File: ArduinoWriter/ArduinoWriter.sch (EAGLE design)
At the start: 11 parts, among them IC1 ATMEGA328-PU, IC2 TC74HC08AP, Q1 HUSG-16.000-20, SW1 SS-12D01-VG4, U1 ARRDUINOUNO-NOSILK

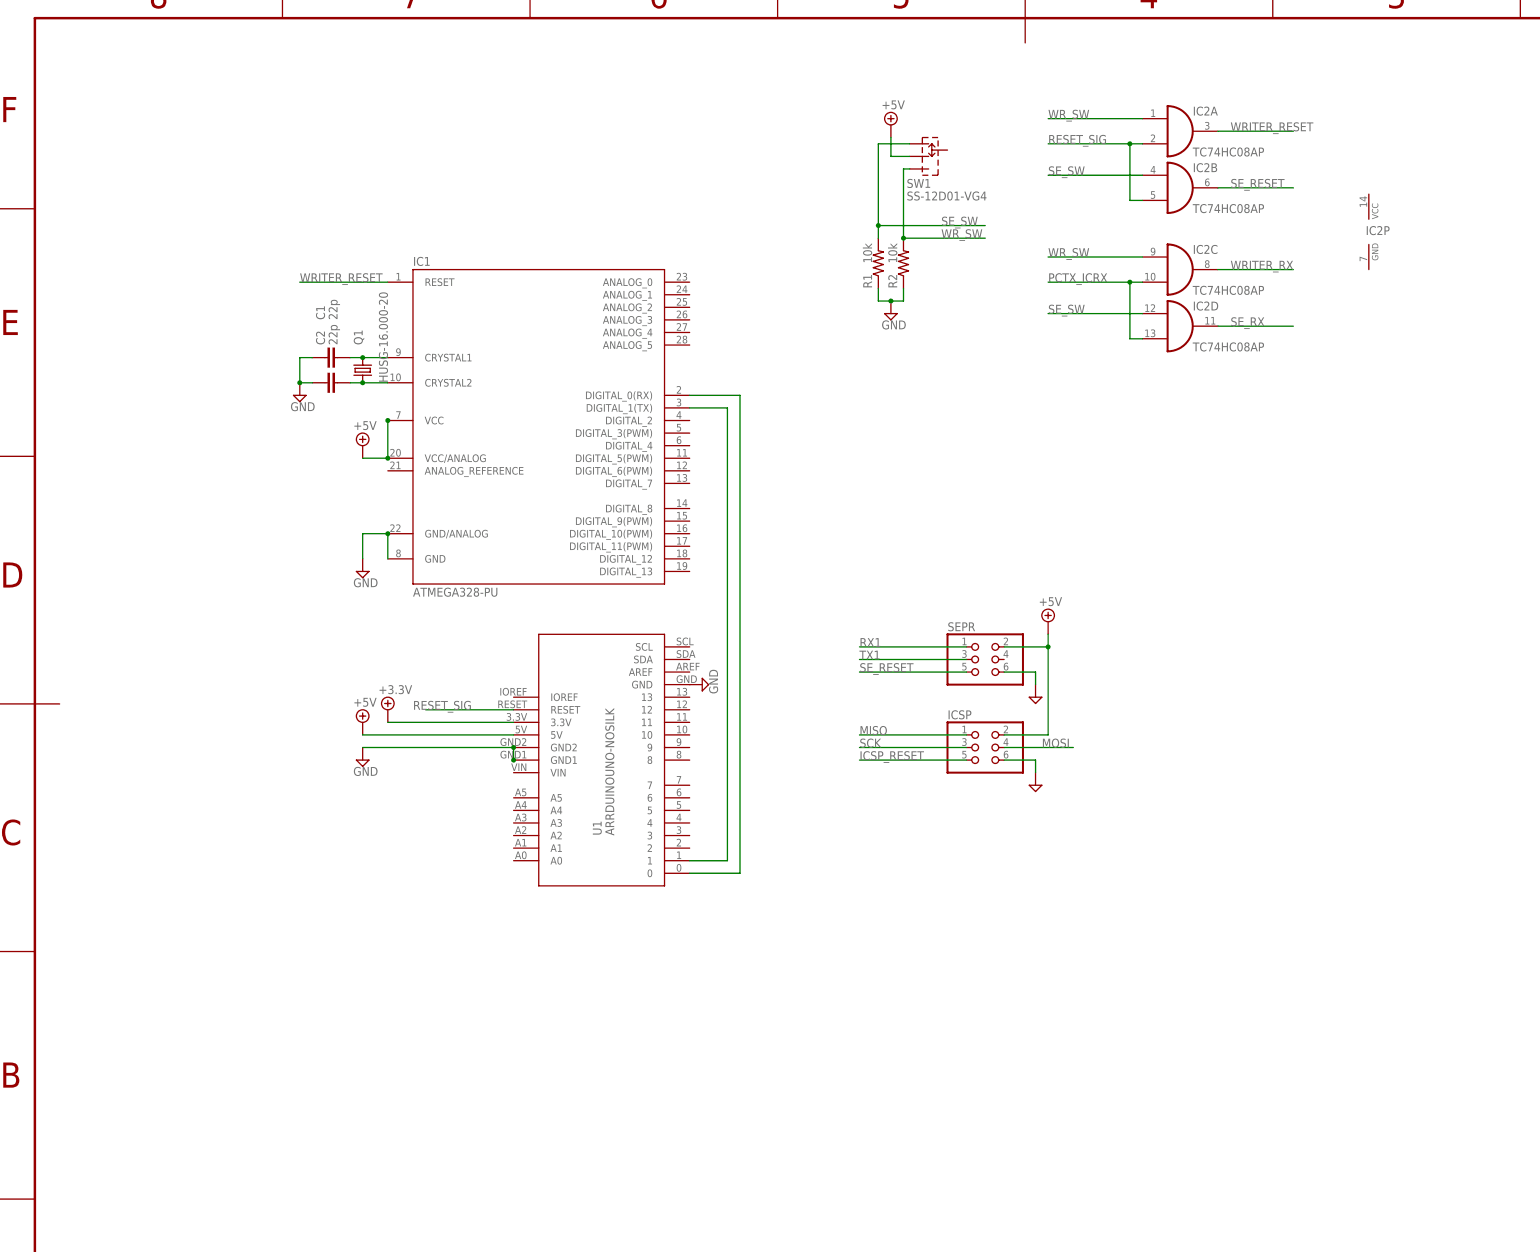
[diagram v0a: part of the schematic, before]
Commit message: SEWR_ICSP 切替回路実装
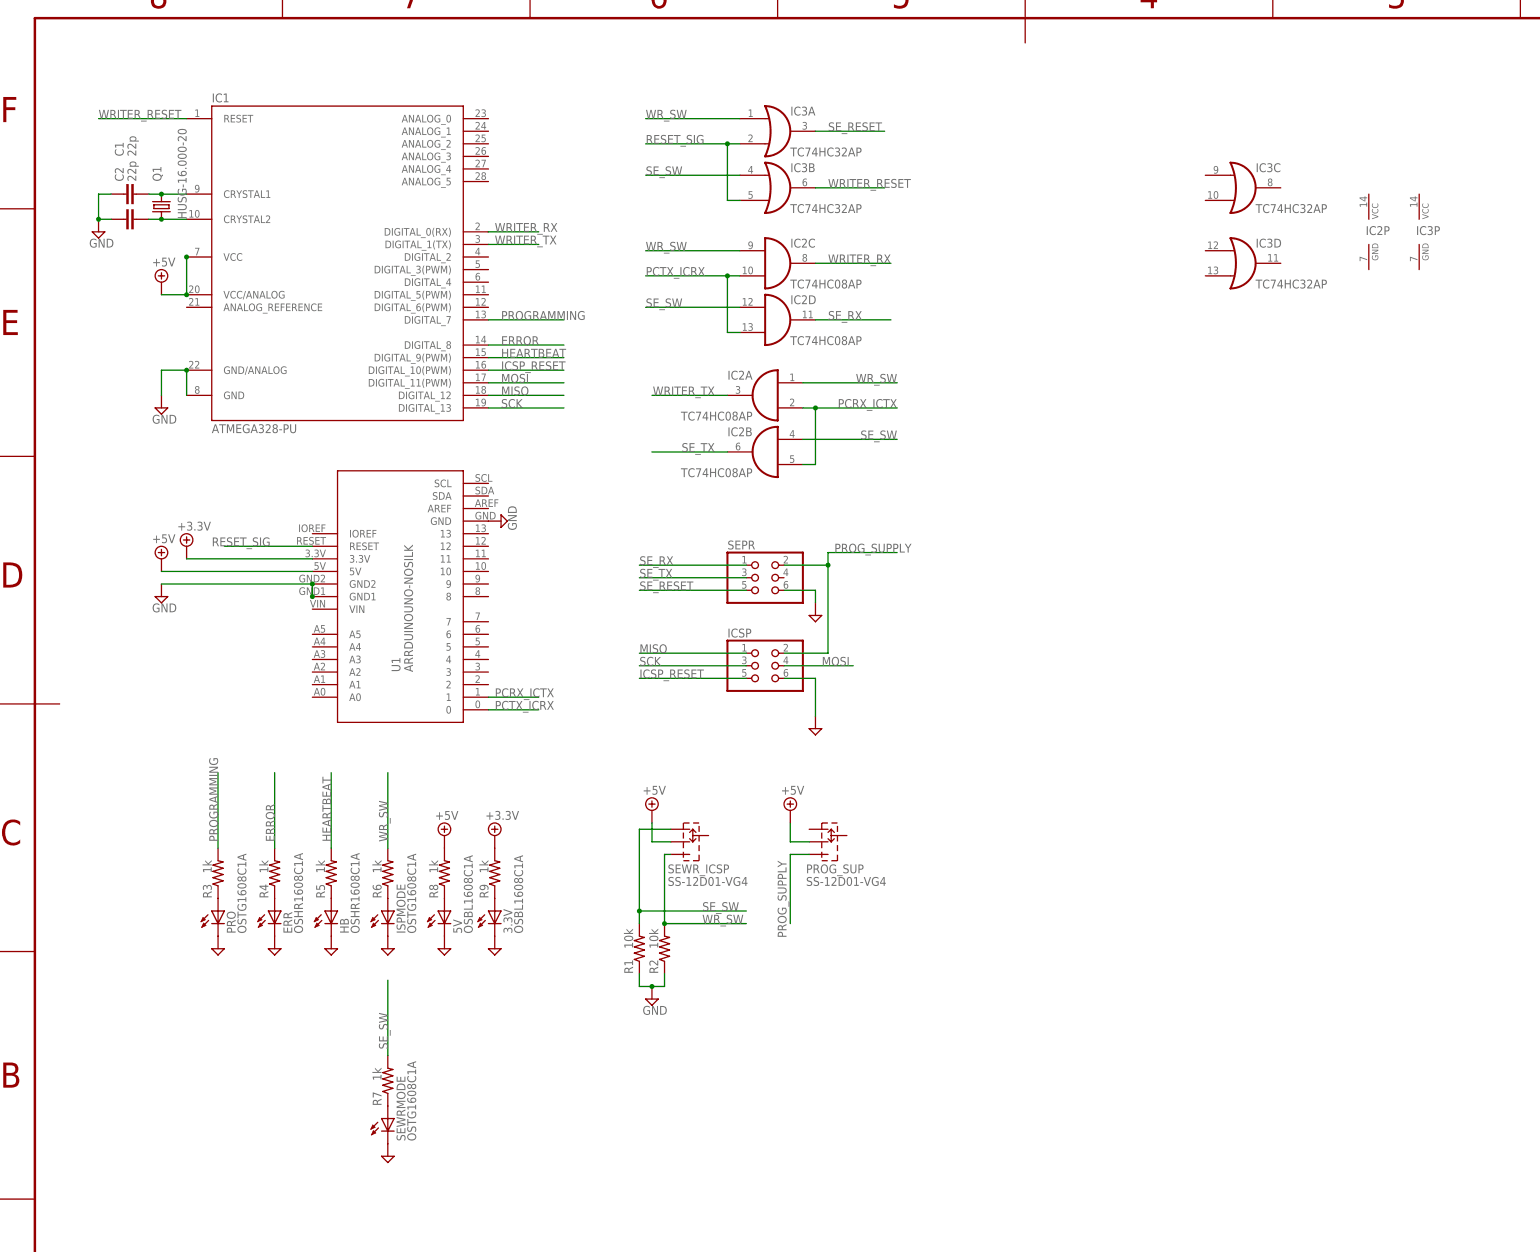
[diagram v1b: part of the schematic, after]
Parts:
- removed SW1: SS-12D01-VG4, スライドスイッチ:SS-12D01-VG4
- added 3.3V, 5V: OSBL1608C1A, LED:OSBL1608C1A
- added ERR, HB: OSHR1608C1A, LED:OSHR1608C1A
- added IC3: TC74HC32AP, 東芝_74LSシリーズ:TC74HC32AP
- added ISPMODE, PRO, SEWRMODE: OSTG1608C1A, LED:OSTG1608C1A
- added PROG_SUP, SEWR_ICSP: SS-12D01-VG4, スライドスイッチ:SS-12D01-VG4
- added R3, R4, R5, R6, R7, R8, R9: 1k, RCL:R1608
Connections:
- removed net RX1: SEPR.1
- removed net TX1: SEPR.3
- new net ERROR: IC1.DIGITAL_8, R4.2
- new net HEARTBEAT: IC1.DIGITAL_9(PWM), R5.2
- new net N$5: HB.A, R5.1
- new net N$6: ISPMODE.A, R6.1
- new net N$7: R7.1, SEWRMODE.A
- new net N$8: 5V.A, R8.1
- new net N$9: 3.3V.A, R9.1
- new net PCRX_ICTX: IC2A.I1, IC2B.I1, U1.1
- new net PROGRAMMING: IC1.DIGITAL_7, R3.2
- new net PROG_SUPPLY: ICSP.2, PROG_SUP.NO, SEPR.2
- new net SE_TX: IC2B.O, SEPR.3
- new net WRITER_TX: IC1.DIGITAL_1(TX), IC2A.O
- net +3.3V: now also R9.2
- net +5V: now also PROG_SUP.COM, R8.2, SEWR_ICSP.COM; no longer ICSP.2, SEPR.2, SW1.COM
- net GND: now also 3.3V.C, 5V.C, ERR.C, HB.C, ISPMODE.C, PRO.C, SEWRMODE.C
- net ICSP_RESET: now also IC1.DIGITAL_10(PWM)
- net MISO: now also IC1.DIGITAL_12
- net MOSI: now also IC1.DIGITAL_11(PWM)
- net N$3: now also PRO.A, R3.1; no longer IC1.DIGITAL_0(RX), U1.0
- net N$4: now also ERR.A, R4.1; no longer IC1.DIGITAL_1(TX), U1.1
- net PCTX_ICRX: now also U1.0
- net RESET_SIG: now also IC3A.I1, IC3B.I1; no longer IC2A.I1, IC2B.I1
- net SCK: now also IC1.DIGITAL_13
- net SE_RESET: now also IC3A.O; no longer IC2B.O
- net SE_RX: now also SEPR.1
- net SE_SW: now also IC3B.I0, R7.2, SEWR_ICSP.NC; no longer SW1.NC
- net WRITER_RESET: now also IC3B.O; no longer IC2A.O
- net WRITER_RX: now also IC1.DIGITAL_0(RX)
- net WR_SW: now also IC3A.I0, R6.2, SEWR_ICSP.NO; no longer SW1.NO
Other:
- moved on the sheet: C1, C2, IC1, IC2A, IC2B, IC2C, IC2D, ICSP, Q1, R1, R2, SEPR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
